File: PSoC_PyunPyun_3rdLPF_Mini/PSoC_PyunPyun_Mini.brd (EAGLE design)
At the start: 57.1 x 52.1 mm, 28 parts, among them IC1 LM358N

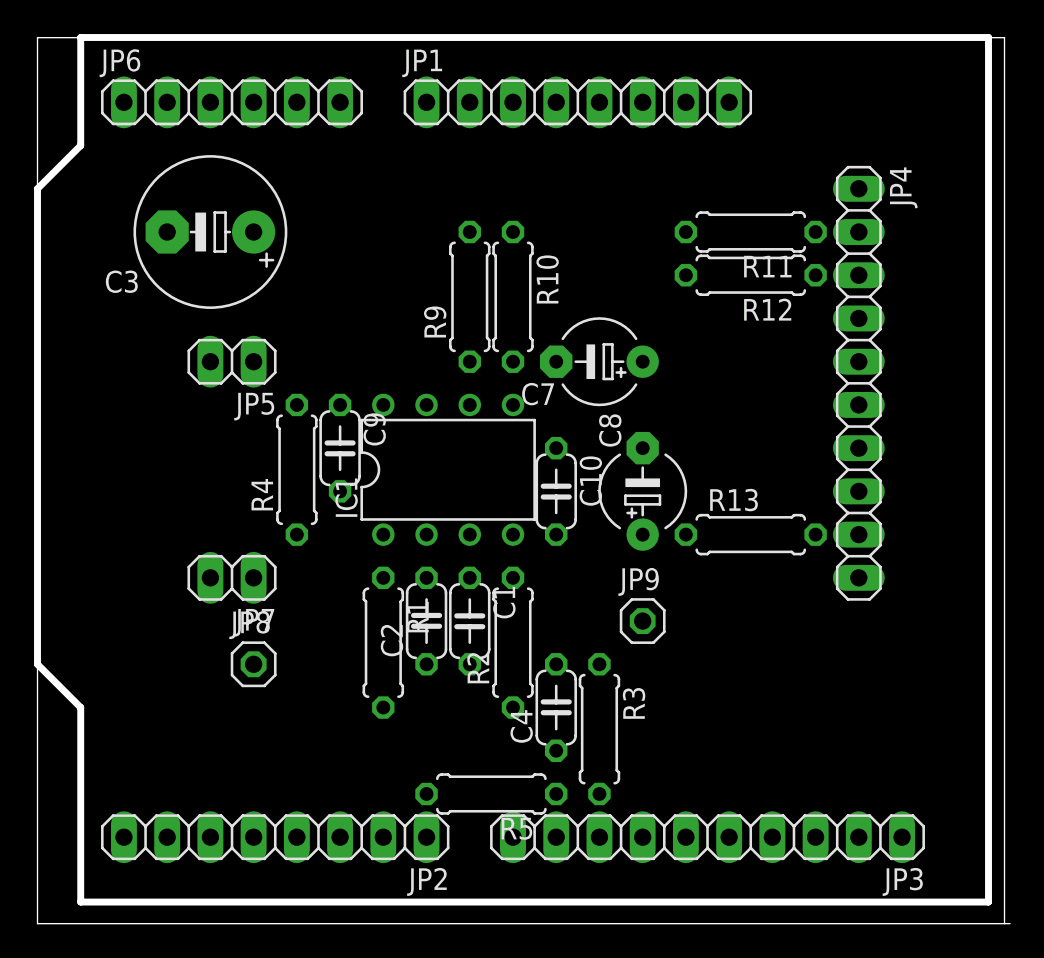
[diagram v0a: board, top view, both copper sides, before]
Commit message: PSoC_PyunPyun_3rdLPF_Mini 回路図修正
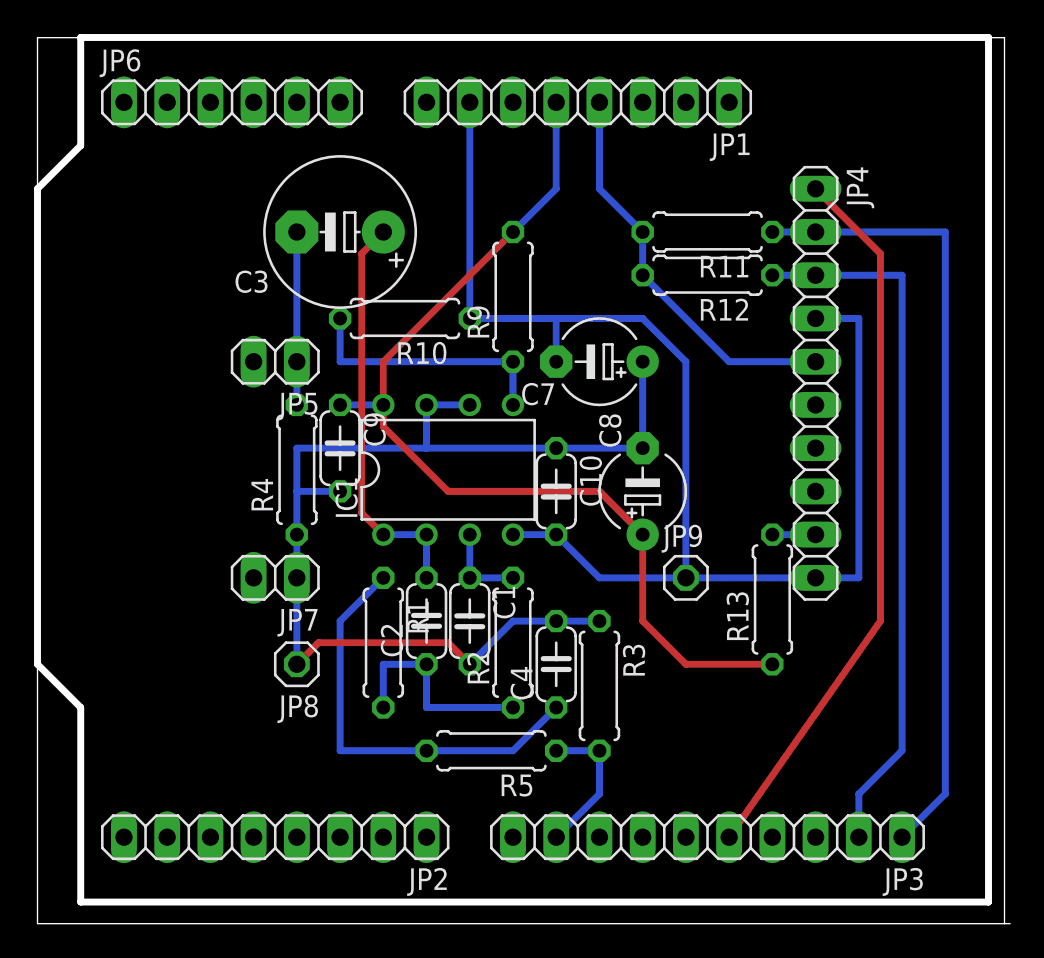
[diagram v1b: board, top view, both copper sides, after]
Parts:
- moved C3 7.62 mm to (17.8, 40.6)
- moved R10 6.48 mm to (21.6, 35.6), turned to 180 degrees
- moved R13 4.02 mm to (43.2, 19.1), turned to 90 degrees
- moved JP9 3.59 mm to (38.1, 20.3)
- moved R9 2.54 mm to (27.9, 36.8)
- moved C4 2.54 mm to (30.5, 15.2)
- moved JP5 2.54 mm to (14.0, 33.0)
- moved JP7 2.54 mm to (14.0, 20.3)
- moved JP8 2.54 mm to (15.2, 15.2), turned to 180 degrees
- moved R3 2.54 mm to (33.0, 14.0)
- moved R5 2.54 mm to (26.7, 10.2)
- moved JP4 2.54 mm to (45.7, 31.8)
- moved R11 2.54 mm to (39.4, 40.6)
- moved R12 2.54 mm to (39.4, 38.1)
- turned JP1 to 180 degrees
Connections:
- net RST: now also JP3.5; no longer JP3.3
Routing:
- net GND: track 0.00 -> 80.8 mm
- net AGND: track 0.00 -> 65.6 mm
- net +5V: track 0.00 -> 57.4 mm
- net SCL: track 0.00 -> 46.8 mm
- net RST: track 0.00 -> 42.5 mm
- net SDA: track 0.00 -> 41.7 mm
- net N$2: track 0.00 -> 25.0 mm
- net N$4: track 0.00 -> 23.9 mm
- net +3.3V: track 0.00 -> 23.5 mm
- net N$8: track 0.00 -> 15.2 mm
- net N$1: track 0.00 -> 12.7 mm
- net N$7: track 0.00 -> 10.2 mm
- net IDAC8: track 0.00 -> 8.67 mm
- net N$3: track 0.00 -> 5.08 mm
- net N$5: track 0.00 -> 2.54 mm
